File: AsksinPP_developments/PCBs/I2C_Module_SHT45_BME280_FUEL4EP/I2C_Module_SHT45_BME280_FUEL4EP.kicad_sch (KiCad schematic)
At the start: 14 parts, among them J1 Conn_01x04, J2 Conn_01x04, U1 BME280, U2 SHT45-AD1B-R2

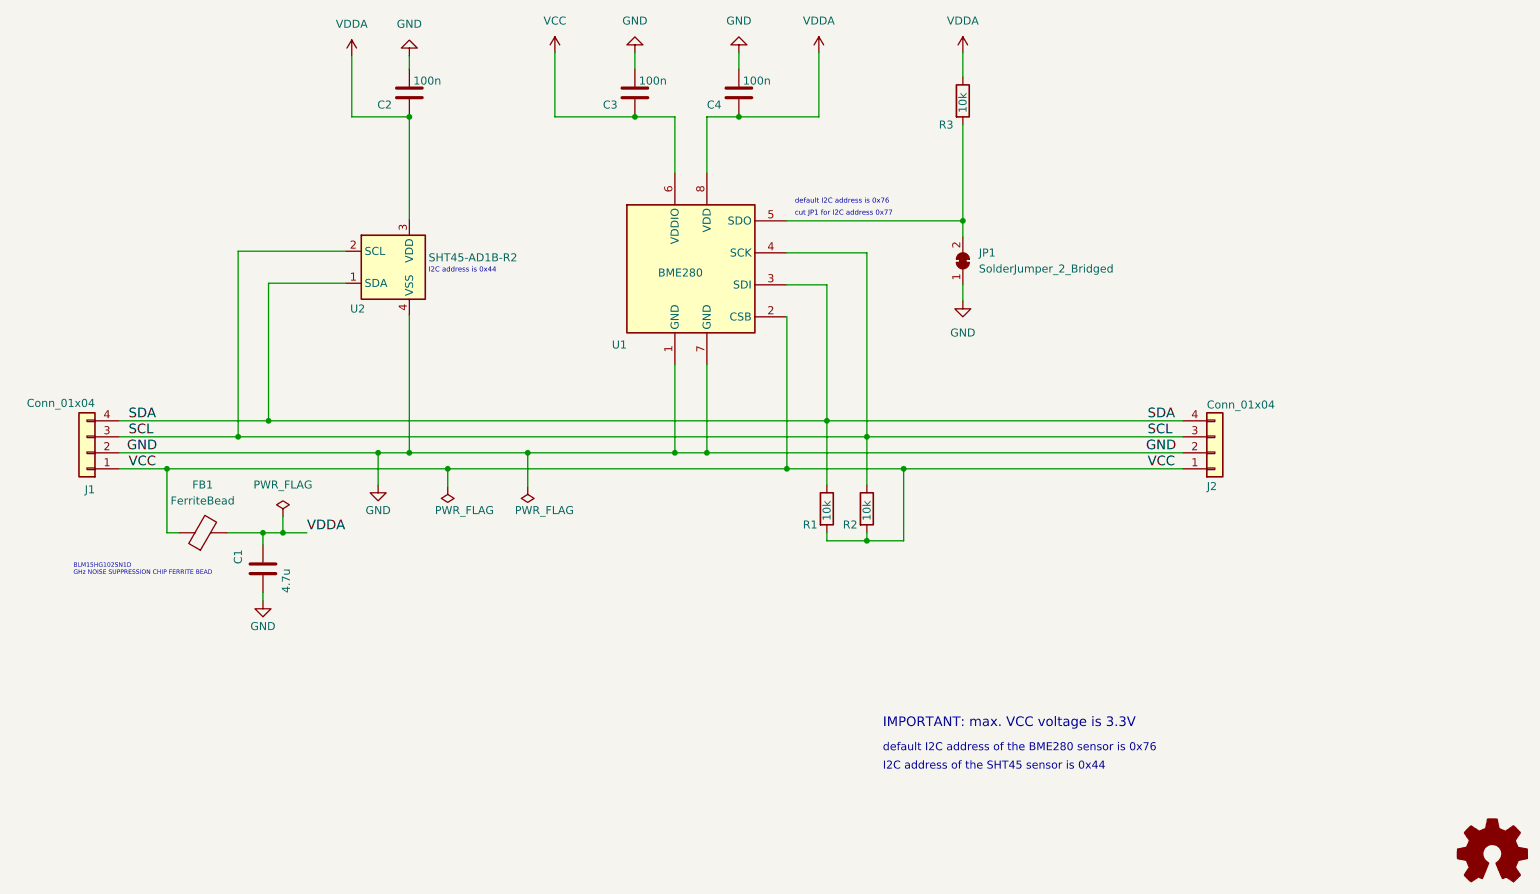
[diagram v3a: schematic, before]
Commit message: PCBs: upgrade some PCBs to KiCAD 7; fix of unnecessary leakage current of I2C address selector: I2C_Module_SHT85_BME280_FUEL4EP, I2C_Module_SHT45_BME280_small_FUEL4EP, I2C_Module_SHT45_BME280_FUEL4EP, I2C_Module_BME280_FUEL4EP, and I2C_Module_BME680_FUEL4EP
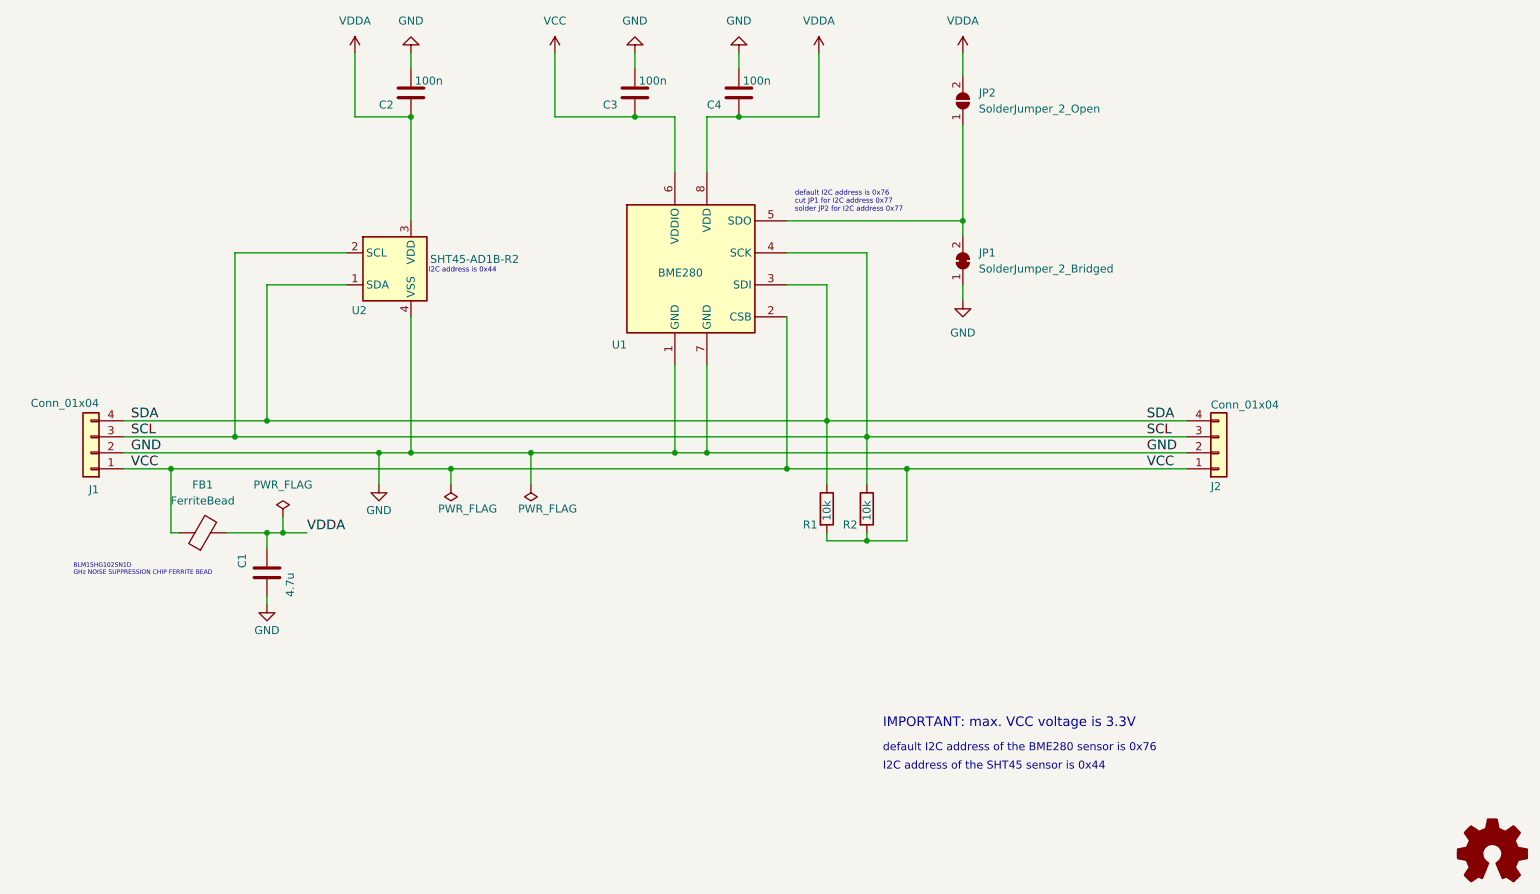
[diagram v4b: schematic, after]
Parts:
- removed R3: 10k, Resistor_SMD:R_0402_1005Metric, symbol Device:R
- added JP2: SolderJumper_2_Open, Jumper:SolderJumper-2_P1.3mm_Open_Pad1.0x1.5mm, symbol Jumper:SolderJumper_2_Open
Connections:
- net VDDA: now also JP2.2 (B)
- net at JP1.2 (B), U1.5 (SDO): now also JP2.1 (A)
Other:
- note added: "solder JP2 for I2C address 0x77"
- moved on the sheet: C1, J1, J2

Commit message: PCBs/I2C_Module_SHT45_BME280_FUEL4EP und PCBs/I2C_Module_BME280_FUEL4EP: migration to KiCAD 8; fix of DRC rules for PCBs/I2C_Module_SHT45_BME280_FUEL4EP
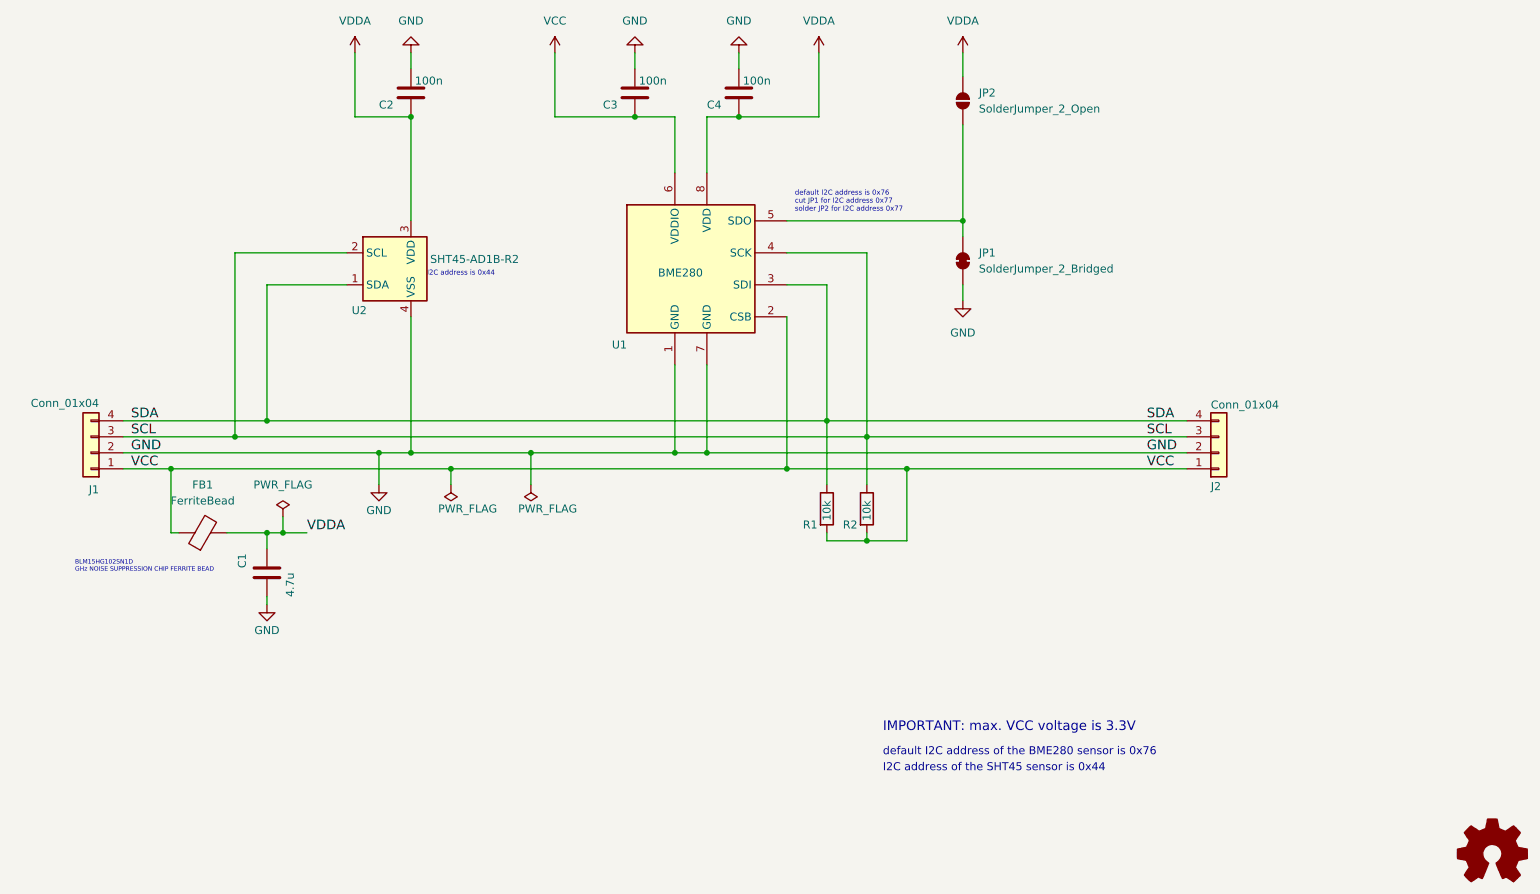
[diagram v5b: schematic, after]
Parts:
- U2: footprint FUEL4EP:SHT4X -> Sensor_Humidity:Sensirion_DFN-4_1.5x1.5mm_P0.8mm_SHT4x_NoCentralPad

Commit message: PCB updates
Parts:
- U2: footprint Sensor_Humidity:Sensirion_DFN-4_1.5x1.5mm_P0.8mm_SHT4x_NoCentralPad -> FUEL4EP:Sensirion_DFN-4_1.5x1.5mm_P0.8mm_SHT4x_NoCentralPad; symbol Sensor_Humidity:SHT4x -> FUEL4EP:SHT4x
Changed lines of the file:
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@@
 	(label "SCL"
 		(at 219.71 109.22 0)
-		(fields_autoplaced yes)
 		(effects
 			(font
@@
 	(label "VCC"
 		(at 219.71 114.3 0)
-		(fields_autoplaced yes)
 		(effects
 			(font
@@
 	(label "VCC"
 		(at 58.42 114.3 0)
-		(fields_autoplaced yes)
 		(effects
 			(font
@@
 	(label "SDA"
 		(at 219.71 106.68 0)
-		(fields_autoplaced yes)
 		(effects
 			(font
@@
 	(label "SCL"
 		(at 58.42 109.22 0)
-		(fields_autoplaced yes)
 		(effects
 			(font
@@
 	(label "GND"
 		(at 58.42 111.76 0)
-		(fields_autoplaced yes)
 		(effects
 			(font
@@
 	(label "VDDA"
 		(at 86.36 124.46 0)
-		(fields_autoplaced yes)
 		(effects
 			(font
@@
 	(label "GND"
 		(at 219.71 111.76 0)
-		(fields_autoplaced yes)
 		(effects
 			(font
@@
 	(label "SDA"
 		(at 58.42 106.68 0)
-		(fields_autoplaced yes)
 		(effects
 			(font
@@
 	)
 	(symbol
-		(lib_id "Sensor_Humidity:SHT4x")
+		(lib_id "FUEL4EP:SHT4x")
 		(at 100.33 82.55 0)
 		(unit 1)
@@
 			)
 		)
-		(property "Footprint" "Sensor_Humidity:Sensirion_DFN-4_1.5x1.5mm_P0.8mm_SHT4x_NoCentralPad"
+		(property "Footprint" "FUEL4EP:Sensirion_DFN-4_1.5x1.5mm_P0.8mm_SHT4x_NoCentralPad"
 			(at 104.14 88.9 0)
 			(effects
@@
 			)
 		)
-		(property "Description" "Digital Humidity and Temperature Sensor, +/-1%RH, +/-0.1degC, I2C, 1.08-3.6V, 16bit, DFN-4"
+		(property "Description" "Digital Humidity and Temperature Sensor, ±1%RH, ±0.1°C, I2C, 1.08-3.6V, 16bit, DFN-4"
 			(at 100.33 82.55 0)
 			(effects
